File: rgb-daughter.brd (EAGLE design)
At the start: 226.1 x 74 mm, 101 parts, among them J1 INPUT

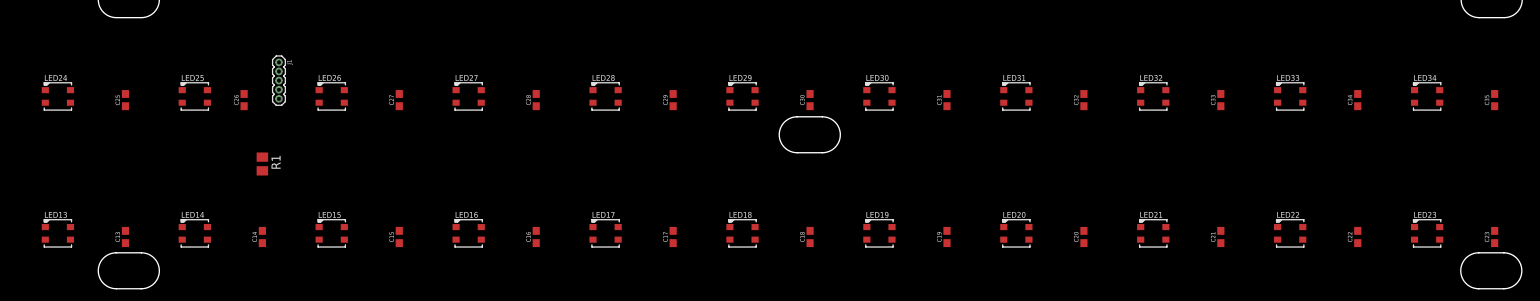
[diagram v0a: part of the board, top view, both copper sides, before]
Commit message: 🚧✨ adds routes
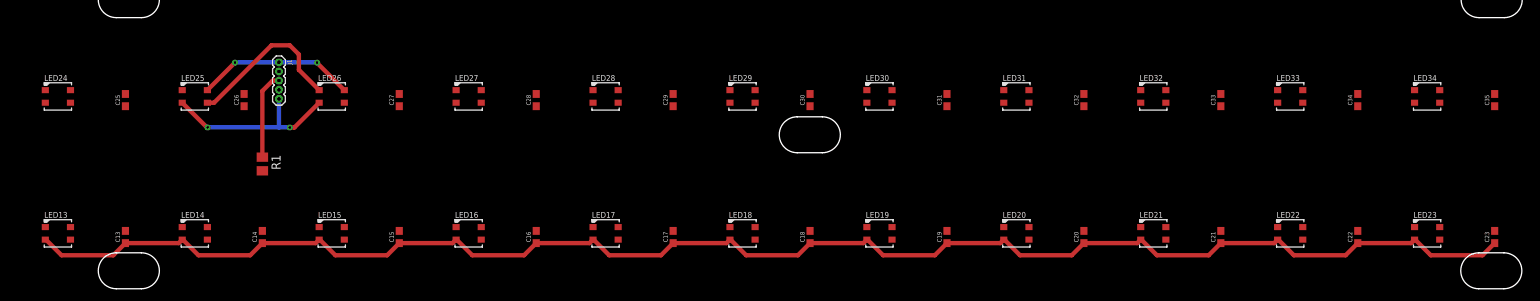
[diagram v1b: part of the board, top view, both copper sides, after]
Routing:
- net VDD: track 0.00 -> 247.2 mm, vias 0 -> 2
- net N$26: track 0.00 -> 22.7 mm
- net GND: track 0.00 -> 22.3 mm, vias 0 -> 2
- net N$3: track 0.00 -> 12.1 mm

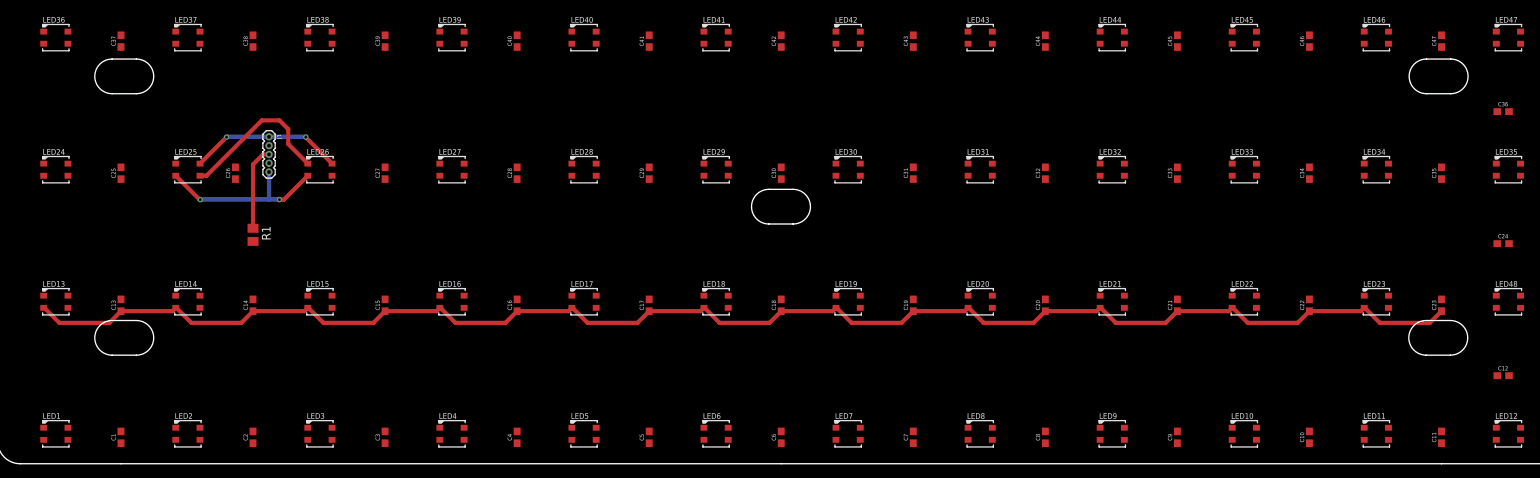
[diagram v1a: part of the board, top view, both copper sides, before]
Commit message: 🚧✨ add VCC routes
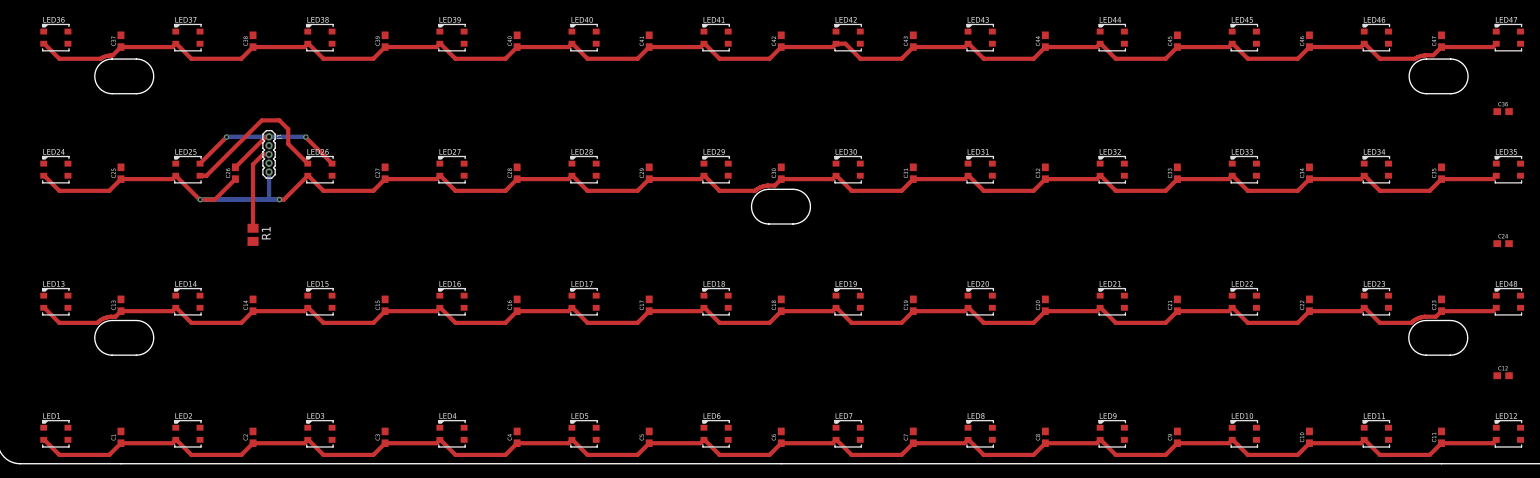
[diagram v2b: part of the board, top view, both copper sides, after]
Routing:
- net VDD: track 247.2 -> 928.2 mm
- net GND: track 22.3 -> 28.9 mm

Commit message: 🚧✨ add GND routes
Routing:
- net GND: track 28.9 -> 953.5 mm

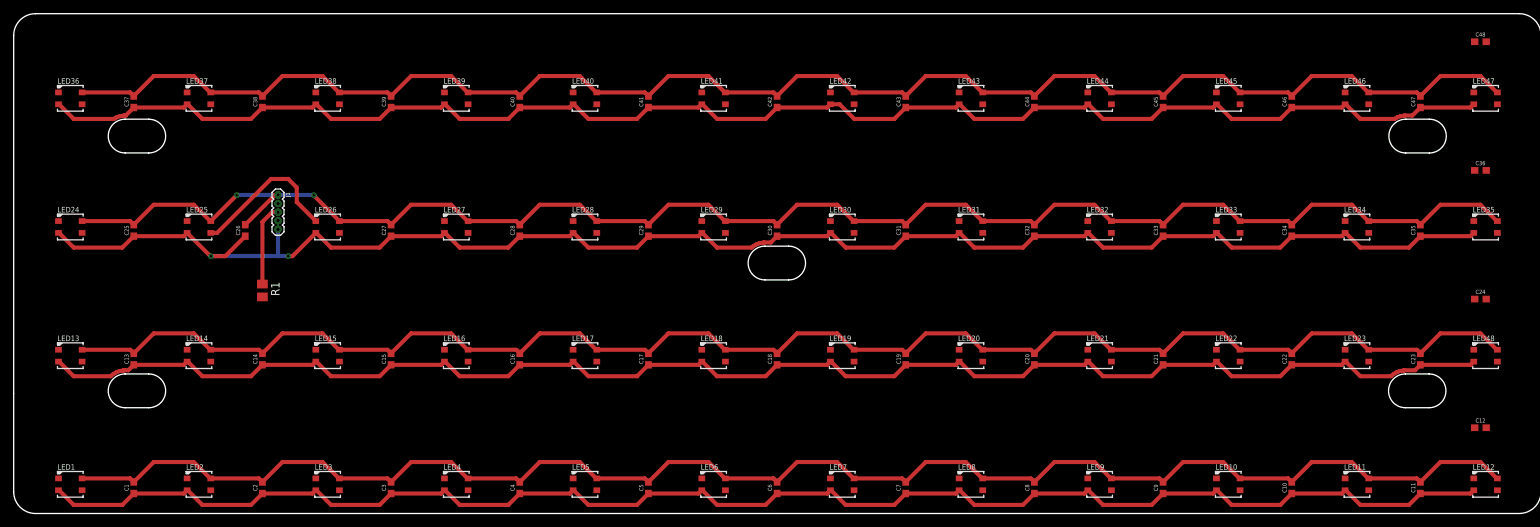
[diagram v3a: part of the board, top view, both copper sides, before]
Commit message: ✨ connect rows with VCC and GND
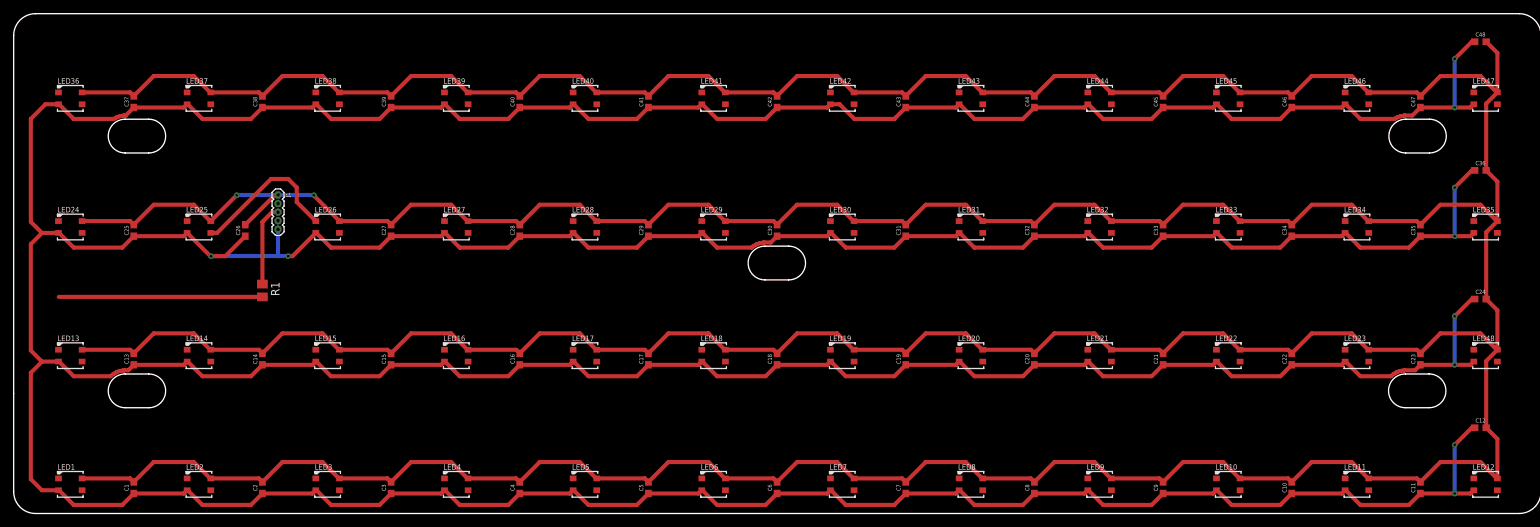
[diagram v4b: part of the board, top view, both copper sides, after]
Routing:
- net VDD: track 928.2 -> 1043.8 mm, vias 2 -> 10
- net GND: track 953.5 -> 1023.0 mm
- net N$1: track 0.00 -> 30.2 mm

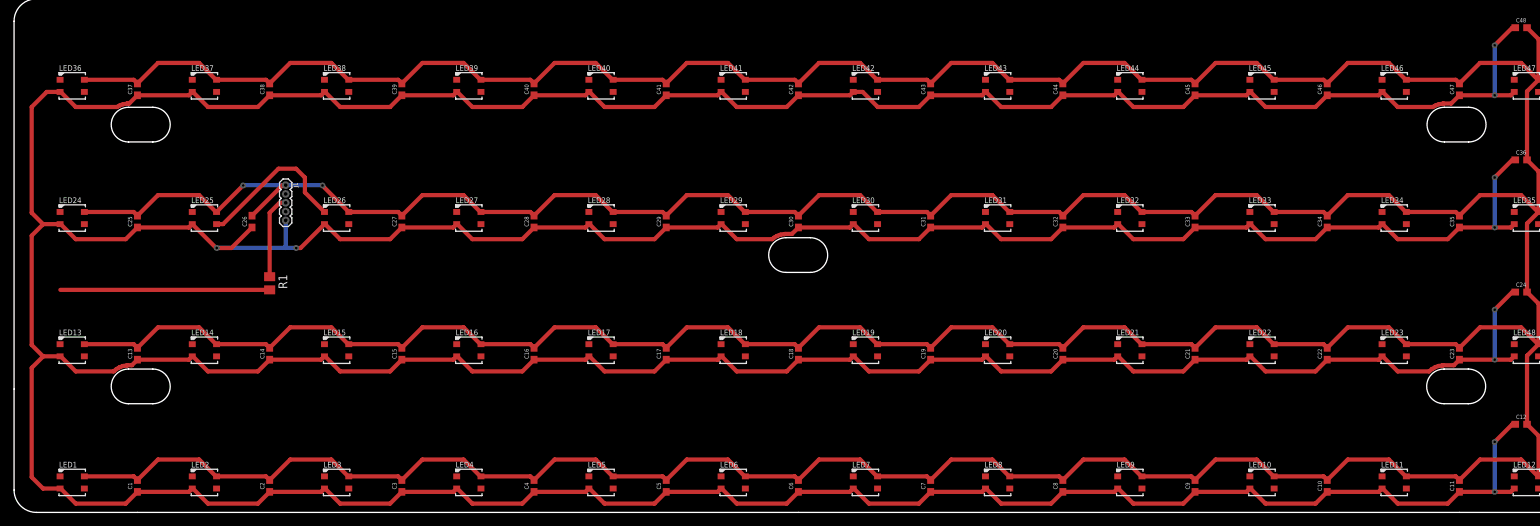
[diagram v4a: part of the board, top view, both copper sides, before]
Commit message: 🚨 resize drill holes
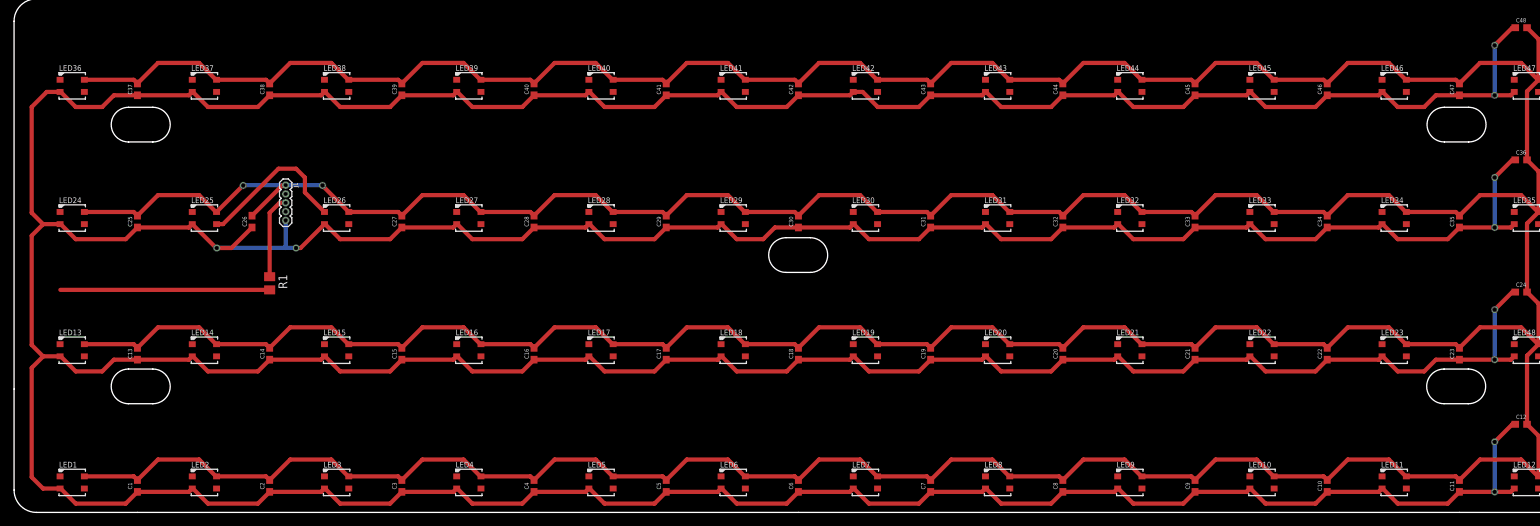
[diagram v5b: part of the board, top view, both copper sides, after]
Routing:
- net VDD: track 1043.8 -> 1044.3 mm
